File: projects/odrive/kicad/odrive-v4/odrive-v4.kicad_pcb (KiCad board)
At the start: 4 copper layers, 170 x 115 mm, 378 parts, among them J1 PC 16/2-ST, J10 ENC_M1_JST-GH, J11 ENC_SPI_JST-GH, J12 GPIO_2x4, J13 BRAKE_EXT, J2 M0 A/B/C, J3 M1 A/B/C, J4 FTSH-105-01-L-DV-K, J5 FAN 12V 150mA MAX, J6 USB4105-GF-A, J7 JST-GH-4 CAN, J8 JST-GH-4 CAN, J9 ENC_M0_JST-GH, Q1 NVMFS5C628NL | BSC027N10NS5, Q10 NVMFS5C628NL, Q11 NVMFS5C628NL, Q12 NVMFS5C628NL, Q13 NVMFS5C628NL, Q14 NVMFS5C628NL, Q15 NVMFS5C628NL, Q16 NVMFS5C628NL, Q17 NVMFS5C628NL, Q18 NVMFS5C628NL, Q19 NVMFS5C628NL, Q20 NVMFS5C628NL, Q21 NVMFS5C628NL, Q30 NVMFS5C628NL, Q31 NVMFS5C628NL, Q32 NVMFS5C628NL, Q33 NVMFS5C628NL, Q34 NVMFS5C628NL, Q35 NVMFS5C628NL, Q36 NVMFS5C628NL, Q37 NVMFS5C628NL, Q38 NVMFS5C628NL, Q39 NVMFS5C628NL, Q40 NVMFS5C628NL, Q41 NVMFS5C628NL, Q50 NVMFS5C628NL/BSC027N10NS5, Q51 NVMFS5C628NL/BSC027N10NS5, SW1 CAN_TERM, U10 TLV9062, U11 TMUX1204, U12 TLV7031, U13 TLV431, U14 74LVC1G04, U15 74LVC1G08, U16 TPD4E05U06, U2 STM32F405RGT6, U20 LM5164DDA, U21 LMR51430, U22 TLV75533PDBV, U23 TPS7A2033DBV, U25 74LVC1G06, U26 TLV7031DBV, U27 74LVC1G08, U28 TPS3840DL30, U3 DRV8353RS, U30 TPS2553DBV, U31 TPS2553DBV, U32 TPS2553DBV, U33 USBLC6-2SC6, U34 TCAN1042HGV, U35 SN74LVC2G17, U36 SN74LVC2G17, U37 SN74LVC2G17, U38 TPD4E05U06, U39 TPD4E05U06, U4 DRV8353RS, U40 SN74LVC1G125, U41 TPD4E05U06, U42 TPD1E10B06, U50 UCC27517A, U51 INA181A2, U52 TLV7031, U53 74LVC1G74, U54 74LVC1G32, U55 74LVC1G08, Y1 8MHz

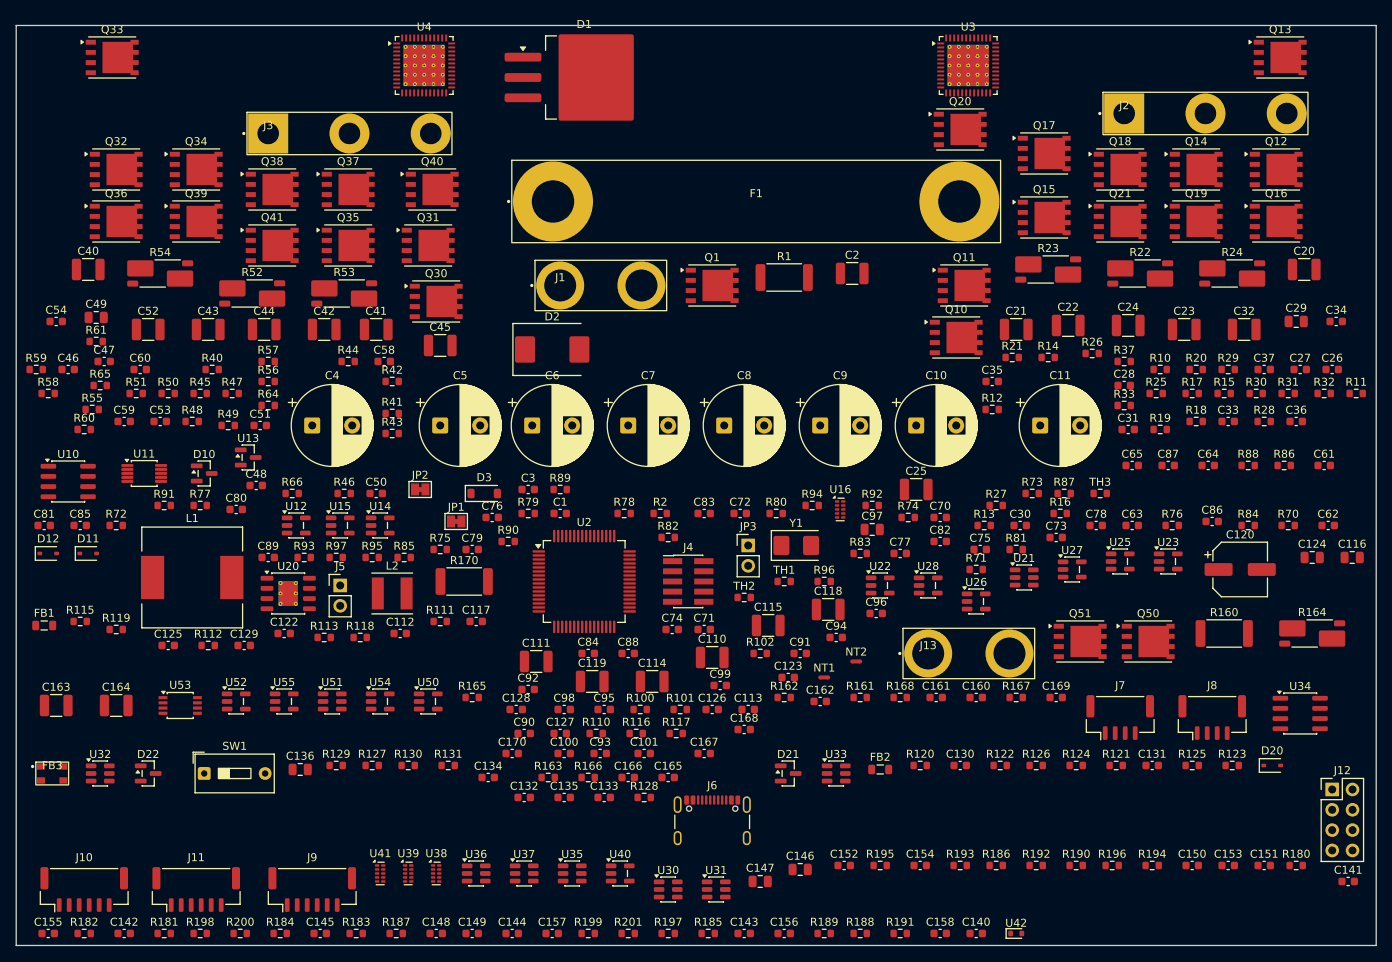
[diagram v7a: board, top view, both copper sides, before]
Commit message: Pour the four-layer plane structure from design doc section 6
Eight zones, filled by KiCad and verified on rendered inner layers: In1.Cu
carries PGND over the power half and GND over the logic half with a 2mm split
between them; In2.Cu carries DCBUS over the power half, an AGND island under
the analog front end (priority 3 so it wins over the pour around it) and a VCC
3V3 pour elsewhere; B.Cu carries the PGND thermal pour under the FET bands for
the heatsink side plus a GND pour under the logic; F.Cu gets a DCBUS pour over
the bulk bank. Grounds stay separate - they meet only at the schematic net
ties, as the audit demanded.

Also corrects the HV netclass clearance from 2.0mm to 0.2mm. The 2mm figure is
the section 6 creepage target for spacing between different nets in routed
copper, but as a netclass clearance KiCad applies it between pads too, and no
real part can satisfy it: a DRV8353 QFN-48 has 0.25mm pad pitch and a 1206 cap
has its own pads 1.8mm apart. That single wrong rule accounted for hundreds of
DRC errors. Creepage now belongs to routing discipline, not to a rule that
declares every power component illegal.
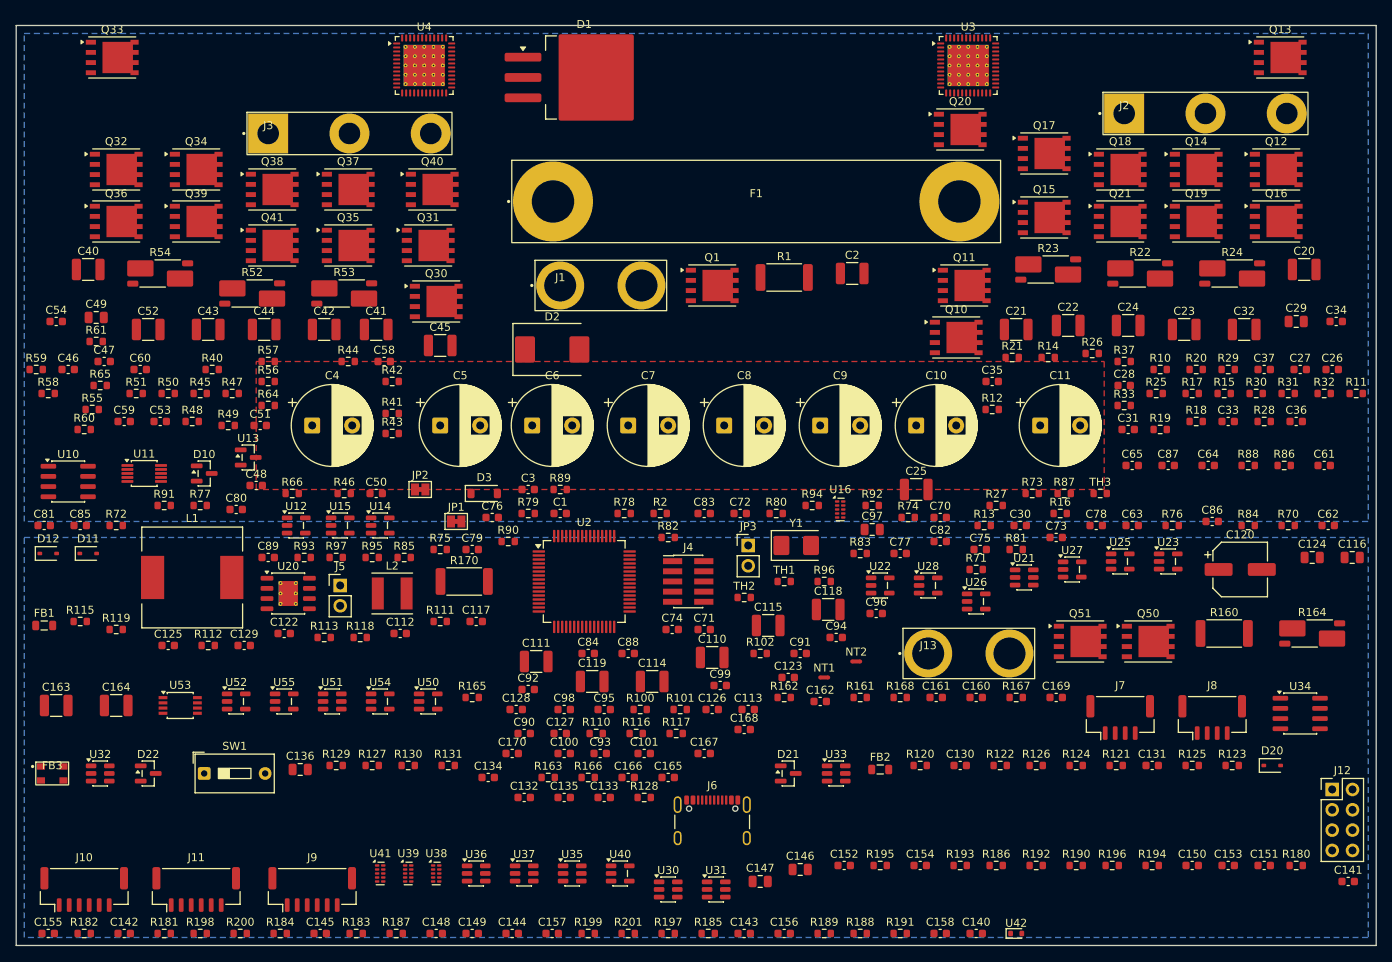
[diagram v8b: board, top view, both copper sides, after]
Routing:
- added copper zone on In2.Cu, net AGND
- added copper zone on F.Cu, net DCBUS
- added copper zone on In2.Cu, net DCBUS
- added copper zone on B.Cu, net GND
- added copper zone on In1.Cu, net GND
- added copper zone on B.Cu, net PGND
- added copper zone on In1.Cu, net PGND
- added copper zone on In2.Cu, net VCC
